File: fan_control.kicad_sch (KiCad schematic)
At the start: 6 parts

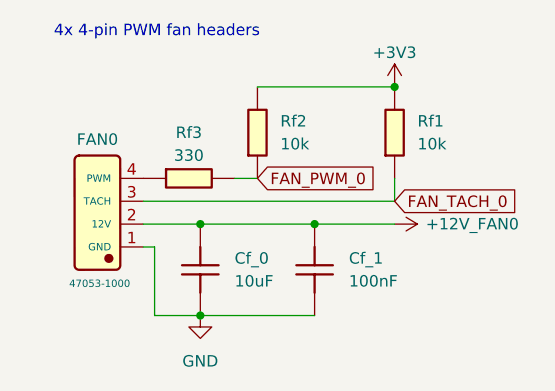
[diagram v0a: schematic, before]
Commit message: Mostly complete initial transfer to hierarchical schematic
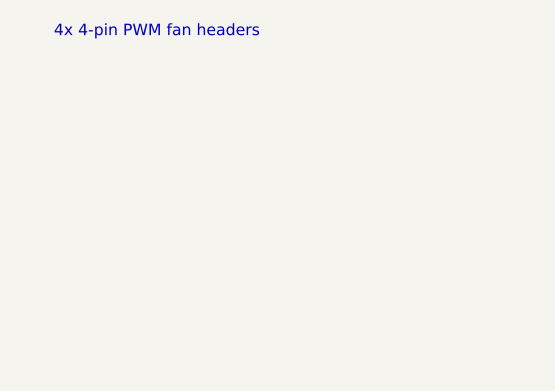
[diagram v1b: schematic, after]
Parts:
- removed Cf_0: 10uF, Capacitor_SMD:C_0603_1608Metric, symbol JLCImport:CL10A106KP8NNNC
- removed Cf_1: 100nF, Capacitor_SMD:C_0402_1005Metric, symbol JLCImport:CL05B104KB54PNC
- removed FAN0: 47053-1000, JLCImport:47053-1000, symbol JLCImport:47053-1000
- removed Rf1, Rf2: 10k, Resistor_SMD:R_0402_1005Metric, symbol JLCImport:0402WGF1002TCE
- removed Rf3: 330, Resistor_SMD:R_0402_1005Metric, symbol JLCImport:0402WGF3300TCE
